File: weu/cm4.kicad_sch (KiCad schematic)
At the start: 4 parts, among them J1 USB_C_Receptacle_USB2.0_14P

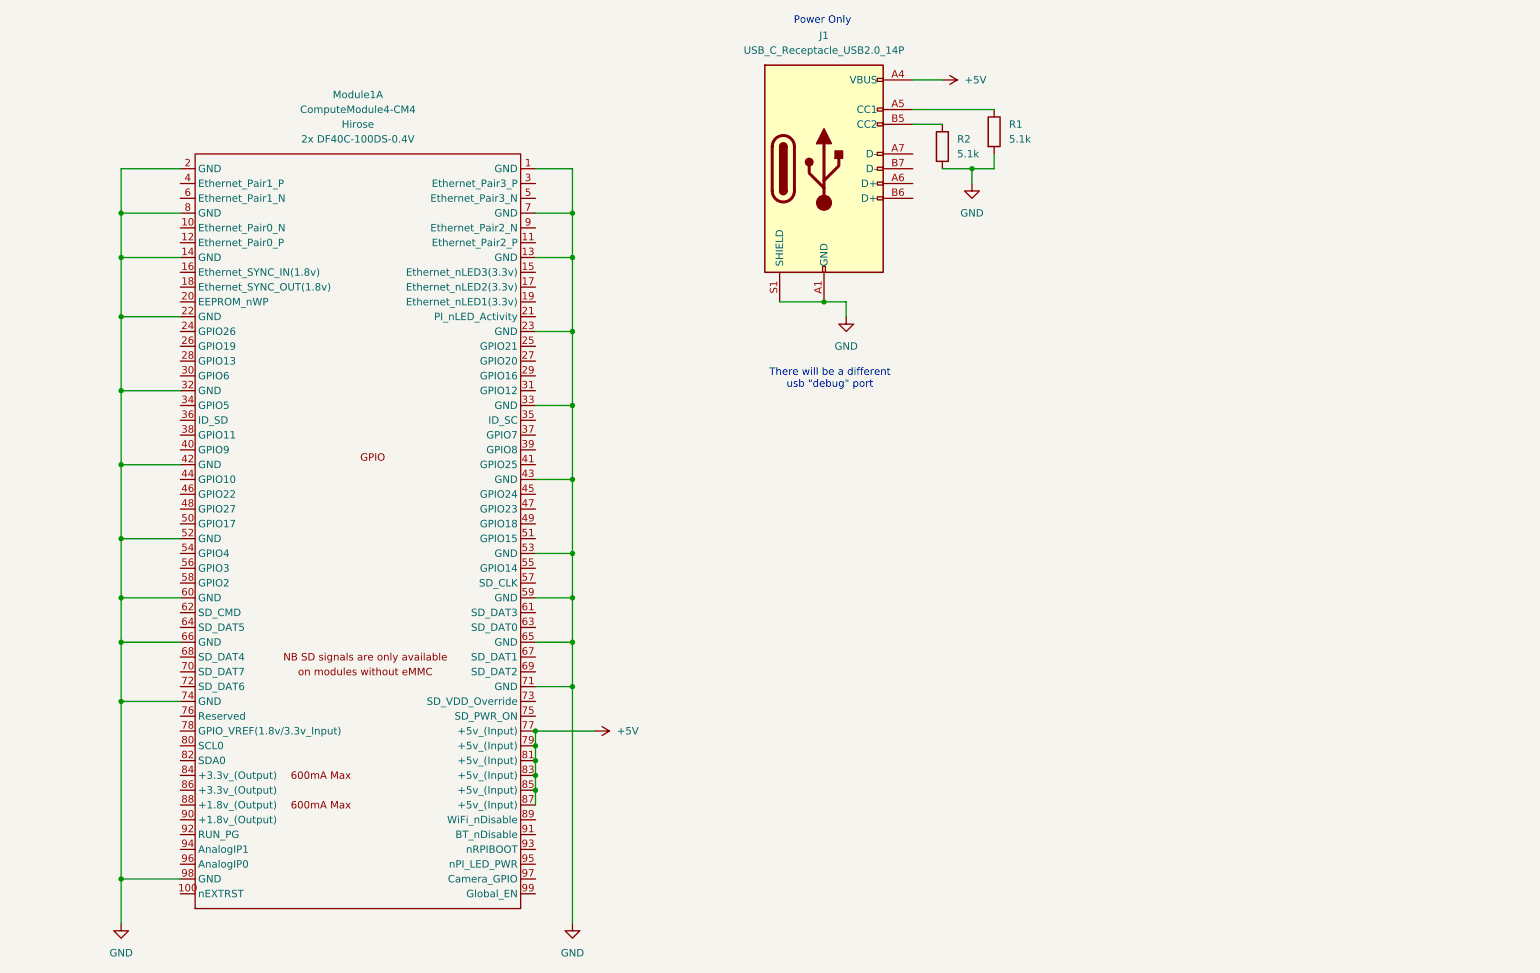
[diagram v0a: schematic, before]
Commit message: added SD card connector
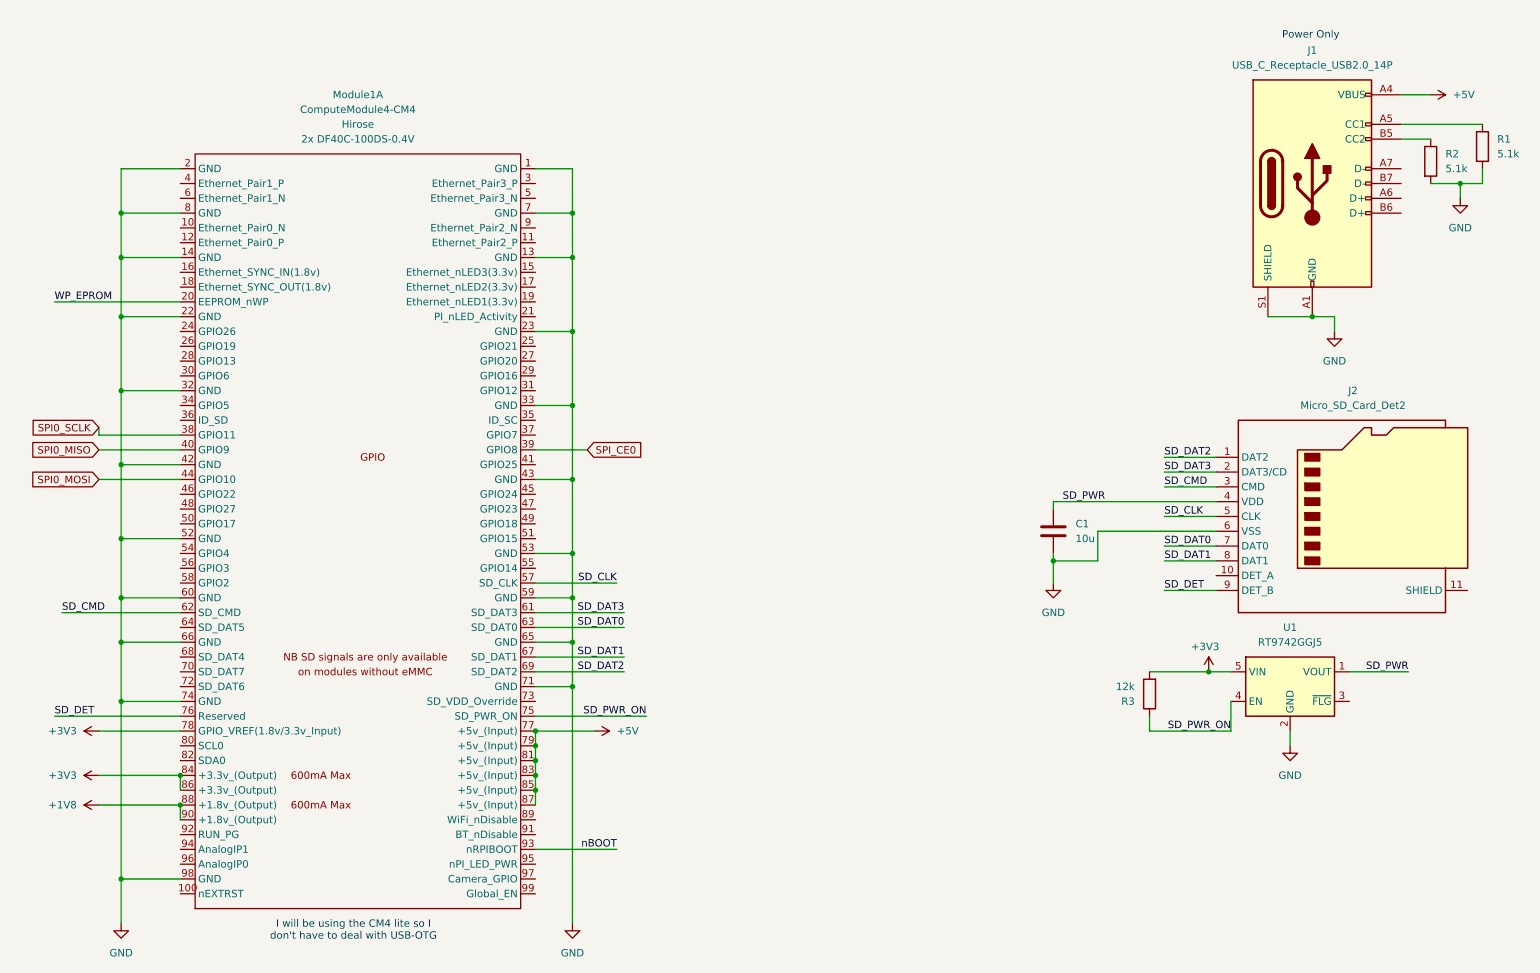
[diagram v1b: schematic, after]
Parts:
- added C1: 10u, symbol Device:C
- added J2: Micro_SD_Card_Det2, symbol Connector:Micro_SD_Card_Det2
- added R3: 12k, symbol Device:R
- added U1: RT9742GGJ5, Package_TO_SOT_SMD:TSOT-23-5, symbol Power_Management:RT9742AGJ5F
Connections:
- net GND: now also C1.2, J2.6 (VSS), U1.2 (GND)
- net WP_EPROM: now reaches Module1.20 (EEPROM_nWP)
- net SPI0_SCLK: now reaches Module1.38 (GPIO11)
- net SPI_CE0: now reaches Module1.39 (GPIO8)
- net SPI0_MISO: now reaches Module1.40 (GPIO9)
- net SPI0_MOSI: now reaches Module1.44 (GPIO10)
- net SD_CLK: now reaches Module1.57 (SD_CLK)
- net SD_CLK: now also J2.5 (CLK)
- net SD_DAT3: now reaches Module1.61 (SD_DAT3)
- net SD_DAT3: now also J2.2 (DAT3/CD)
- net SD_CMD: now reaches Module1.62 (SD_CMD)
- net SD_CMD: now also J2.3 (CMD)
- net SD_DAT0: now reaches Module1.63 (SD_DAT0)
- net SD_DAT0: now also J2.7 (DAT0)
- net SD_DAT1: now reaches Module1.67 (SD_DAT1)
- net SD_DAT1: now also J2.8 (DAT1)
- net SD_DAT2: now reaches Module1.69 (SD_DAT2)
- net SD_DAT2: now also J2.1 (DAT2)
- net SD_PWR_ON: now reaches Module1.75 (SD_PWR_ON)
- net SD_PWR_ON: now also R3.1, U1.4 (EN)
- net SD_DET: now reaches Module1.76 (Reserved)
- net SD_DET: now also J2.9 (DET_B)
- net +3V3: now reaches Module1.78 (GPIO_VREF(1.8v/3.3v_Input))
- net +3V3: now also Module1.84 (+3.3v_(Output)), Module1.86 (+3.3v_(Output)), R3.2, U1.5 (VIN)
- net +1V8: now reaches Module1.88 (+1.8v_(Output))
- net +1V8: now also Module1.90 (+1.8v_(Output))
- net nBOOT: now reaches Module1.93 (nRPIBOOT)
- new net SD_PWR: C1.1, J2.4 (VDD), U1.1 (VOUT)
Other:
- note added: "I will be using the CM4 lite so I don't have to deal with USB-OTG"
- note removed: "There will be a different usb "debug" port"
- moved on the sheet: J1, R1, R2
